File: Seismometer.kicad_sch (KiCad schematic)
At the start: 32 parts

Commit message: Finishing schematic
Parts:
- removed R?: 51, symbol Device:R
- removed R?: R, symbol Device:R
- removed U?: ESP32-WROOM-32, RF_Module:ESP32-WROOM-32, symbol RF_Module:ESP32-WROOM-32
- added C1, C2, C3, C4: 100n, Capacitor_SMD:C_0603_1608Metric_Pad1.08x0.95mm_HandSolder, symbol Device:C
- added R1, R2: 10k, Resistor_SMD:R_0603_1608Metric, symbol Device:R
- added R10, R11, R12, R13, R14, R15, R16, R17, R18, R19, R20, R21, R22, R23, R24, R25, R26, R27, R28, R29, R31, R32, R33, R34, R35, R36, R37, R38, R39, R4, R5, R6, R7, R8, R9: 51, Resistor_SMD:R_0603_1608Metric, symbol Device:R
- added R3, R30: 100k, Resistor_SMD:R_0603_1608Metric, symbol Device:R
- added U1: DLVR-F50D, Package_DIP:DIP-8_W8.89mm_SMDSocket_LongPads, symbol seismometer:DLVR
- C10, C11, C13, C6, C7, C8: renamed from C?; footprint (none) -> Capacitor_SMD:C_0603_1608Metric_Pad1.08x0.95mm_HandSolder
- C12, C14, C15, C5, C9: renamed from C?; footprint (none) -> Capacitor_SMD:C_0805_2012Metric
- FB1, FB2: renamed from FB?; footprint (none) -> Inductor_SMD:L_0805_2012Metric
- R40, R41, R43, R44, R45, R46, R47, R48, R49, R50: renamed from R?; footprint (none) -> Resistor_SMD:R_0603_1608Metric
- R42: renamed from R?; value 51 -> 100k; footprint (none) -> Resistor_SMD:R_0603_1608Metric
- U5: renamed from U?; footprint (none) -> seismometer:Teensy41
- gave numbers to parts that had none: 4
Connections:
- net +3V3: now also C13.1, R49.1, X1.4 (Vdd), C1.1, R1.2, R2.2, R3.2, U1.2 (VSS)
- net GND: now also U3.10 (AIN3P), U3.9 (AIN3N), U5.1 (GND), U5.34 (GND), U5.47 (GND), C1.2, C2.2, C3.2, C4.2, R10.1, R11.1, R12.1, R13.1, R14.1, R15.1, R16.1, R17.1, R18.1, R19.1, R20.1, R21.1, R22.1, R23.2, R24.2, R25.2, R26.2, R27.2, R28.2, R29.2, R30.1, R31.2, R32.2, R33.2, R34.2, R35.2, R36.2, R37.2, R38.2, R7.1, R8.1, R9.1, U1.1 (GND)
- net MISO: now also R45.2, U5.14 (12_MISO_MQSL)
- net MOSI: now also R50.1, U3.16 (DIN)
- net SCK: now also U3.14 (SCLK), R4.2
- net at R47.2: now also U5.20 (28_RX7); no longer U5.18 (26_A12_MOSI1)
- net at U2.11 (~{INT2}): now also R30.2
- net INT_ACCEL: now reaches R43.2
- net INT_ACCEL: now also U5.2 (0_RX1_CRX2_CS1)
- net at U5.10 (8_TX2_IN1): now also R13.2
- net at U5.11 (9_OUT1C): now also R14.2
- net at U5.12 (10_CS_MQSR): now also R15.2
- net 3V3_TEENSY: now reaches U5.15 (3V3)
- net 3V3_TEENSY: now also U5.46 (3V3), C3.1, C4.1
- net at U5.16 (24_A10_TX6_SCL2): now also R46.2
- net at U5.17 (25_A11_RX6_SDA2): now also R16.2
- net at U5.19 (27_A13_SCK1): now also R18.2
- net at U5.21 (29_TX7): now also R19.2
- net at U5.22 (30_CRX3): now also R20.2
- net at U5.23 (31_CTX3): now also R21.2
- net at U5.24 (32_OUT1B): now also R22.2
- net at U5.25 (33_MCLK2): now also R23.1
- net at U5.26 (34_RX8): now also R24.1
- net at U5.27 (35_TX8): now also R25.1
- net at U5.28 (36_CS): now also R6.1
- net at U5.29 (37_CS): now also R5.1
- net INT_DLVR: now reaches U5.3 (1_TX1_CTX2_MISO1)
- net INT_DLVR: now also R3.1, R39.1
- net at U5.30 (38_CS1_IN1): now also R26.1
- net at U5.31 (39_MISO1_OUT1A): now also R27.1
- net at U5.32 (40_A16): now also R28.1
- net at U5.33 (41_A17): now also R29.1
- net at U5.35 (13_SCK_LED): now also R4.1
- net at U5.36 (14_A0_TX3_SPDIF_OUT): now also R31.1
- net at U5.37 (15_A1_RX3_SPDIF_IN): now also R32.1
- net at U5.38 (16_A2_RX4_SCL1): now also R33.1
- net at U5.39 (17_A3_TX4_SDA1): now also R34.1
- net at U5.4 (2_OUT2): now also R7.2
- net SDA: now reaches U5.40 (18_A4_SDA)
- net SDA: now also R2.1, U1.3 (SDA/MISO)
- net SCL: now reaches U5.41 (19_A5_SCL)
- net SCL: now also R1.1, U1.4 (SCL/SCKL)
- net at U5.42 (20_A6_TX5_LRCLK1): now also R35.1
- net at U5.43 (21_A7_RX5_BCLK1): now also R36.1
- net at U5.44 (22_A8_CTX1): now also R37.1
- net at U5.45 (23_A9_CRX1_MCLK1): now also R38.1
- net at U5.48 (VIN): now also C2.1
- net at U5.5 (3_LRCLK2): now also R8.2
- net at U5.6 (4_BCLK2): now also R9.2
- net at U5.7 (5_IN2): now also R10.2
- net at U5.8 (6_OUT1D): now also R11.2
- net at U5.9 (7_RX2_OUT1A): now also R12.2
- net ~{CS_ADC}: now reaches U3.12 (CS)
- net ~{CS_ADC}: now also R6.2
- net ~{CS ACCEL} renamed ~{CS_ACCEL}
- net ~{CS_ACCEL}: now also R5.2
- new net: R17.2, U5.18 (26_A12_MOSI1)
- new net: R39.2, U1.5 (INT/SS)
- now unconnected: U2.10 (NC), U2.5 (NC), U2.8 (NC)
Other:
- moved on the sheet: C11, C12, C13, C14, C15, FB2, R44, R46, R47, R48, R49, R50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

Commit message: Layout
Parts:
- FB1, FB2: value FerriteBead_Small -> MPZ1608S102ATA00; MANUFACTURER (none) -> TDK
- R41: value 4k7 -> 100k
- U2: footprint MC3479:PQFN50P200X200X100-12N -> seismometer:PQFN50P200X200X100-12N
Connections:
- net at C15.1, FB2.1: now also C2.1, U5.48 (VIN); no longer U5.49 (VUSB)
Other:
- moved on the sheet: C7, FB1

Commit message: Initial layout complete
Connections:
- net GND: now also C4.1, R25.1, R6.1; no longer C4.2, R21.1, R25.2
- net INT_ACCEL: now also U5.24 (32_OUT1B); no longer U5.2 (0_RX1_CRX2_CS1)
- net ~{CS_ACCEL}: now also R21.1; no longer R5.2
- net ~{CS_ADC}: now also R5.2; no longer R6.2
- net at U5.20 (28_RX7): now also R6.2; no longer R47.2
- net ADC_SYNC/RESET: now reaches U5.28 (36_CS)
- net ADC_SYNC/RESET: now also R47.2; no longer R6.1
- net at U5.16 (24_A10_TX6_SCL2): now also R25.2; no longer R46.2
- net at R22.2: now also U5.2 (0_RX1_CRX2_CS1); no longer U5.24 (32_OUT1B)
- net ADC_DRDY: now reaches U5.27 (35_TX8)
- net ADC_DRDY: now also R46.2; no longer R25.1
- net 3V3_TEENSY: no longer names the net of C3.1, U5.46 (3V3)
- net 3V3_TEENSY: no longer C4.1, U5.15 (3V3)
- new net: C4.2, U5.15 (3V3)
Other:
- moved on the sheet: C3, C4, R5, R50, R6

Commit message: Ready
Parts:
- C1, C10, C13, C2, C3, C4, C6, C7: MANUFACTURER (none) -> KEMET; MP (none) -> CGA3E3X7R1H224K080AB
- C11: value 10p -> 12p; MANUFACTURER (none) -> KEMET; MP (none) -> C0603C120J5GACTU
- C12, C14, C15, C5, C9: MANUFACTURER (none) -> YAEGO; MP (none) -> CC0402KRX5R6BB105
- C8: MANUFACTURER (none) -> TDK; MP (none) -> CGA3E3X7R1H224K080AB
- FB1, FB2: MP (none) -> MPZ1608S102ATA00
- R1, R2: MANUFACTURER (none) -> PANASONIC; MP (none) -> ERJ3EKF1002V
- R10, R11, R12, R13, R14, R15, R16, R17, R18, R19, R20, R21, R22, R23, R24, R25, R26, R27, R28, R29, R31, R32, R33, R34, R35, R36, R37, R38, R39, R4, R40, R43, R45, R46, R47, R5, R50, R6, R7, R8, R9: MANUFACTURER (none) -> YAGEO; MP (none) -> RC0603FR-0751RL
- R3, R30, R41, R42, R48, R49: MANUFACTURER (none) -> VISHAY; MP (none) -> CRCW0603100KFKEA
- R44: MANUFACTURER (none) -> VISHAY; MP (none) -> CRCW060310R0FKEA
- U1: MANUFACTURER (none) -> AllSensors; MP (none) -> DLVR-F50D; now not fitted; now left out of the parts list
- U2: Purchase-URL https://www.snapeda.com/api/url_track_click_mouser/?unipart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 -> (none); SnapEDA_Link https://www.snapeda.com/parts/MC3479/Memsic/view-part/?ref=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 -> (none)
- U3: MANUFACTURER (none) -> Texas Instruments; MP (none) -> ADS131M04-Q1
- U4: MANUFACTURER (none) -> Texas Instruments; MP (none) -> LP5907MFX-3.3
- U5: MANUFACTURER (none) -> PRJC; now not fitted; now left out of the parts list
- X1: value ASE-xxxMHz -> SIT8924BA-22-33E-8.192000G; MANUFACTURER (none) -> SiTime; MP (none) -> SIT8924BA-22-33E-8.192000G

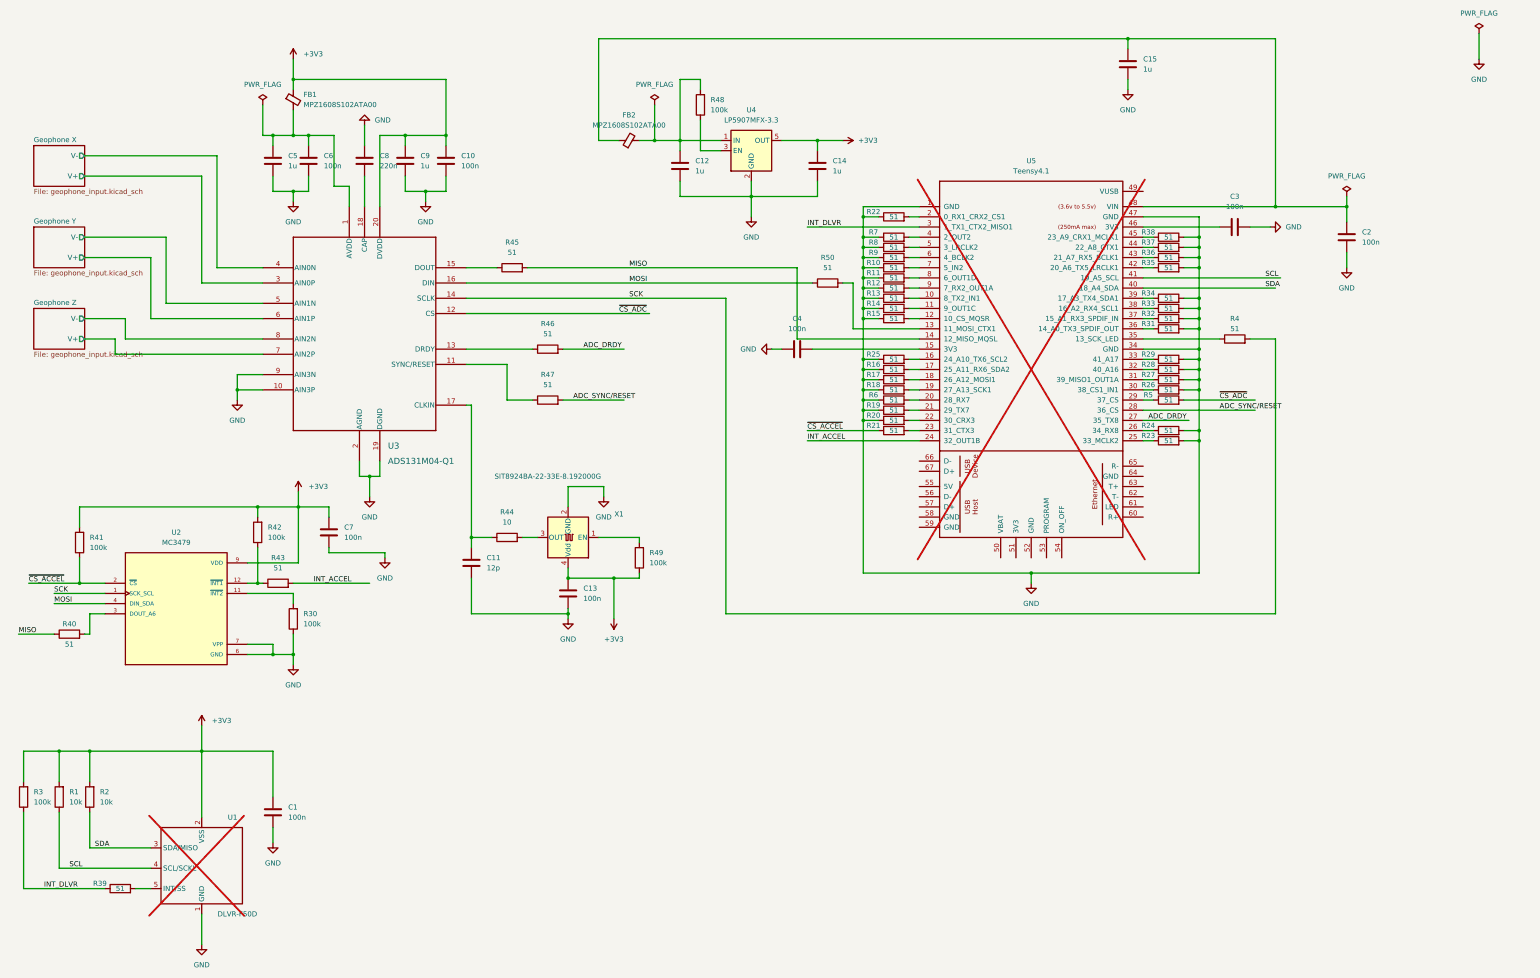
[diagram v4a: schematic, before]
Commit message: Active input filter
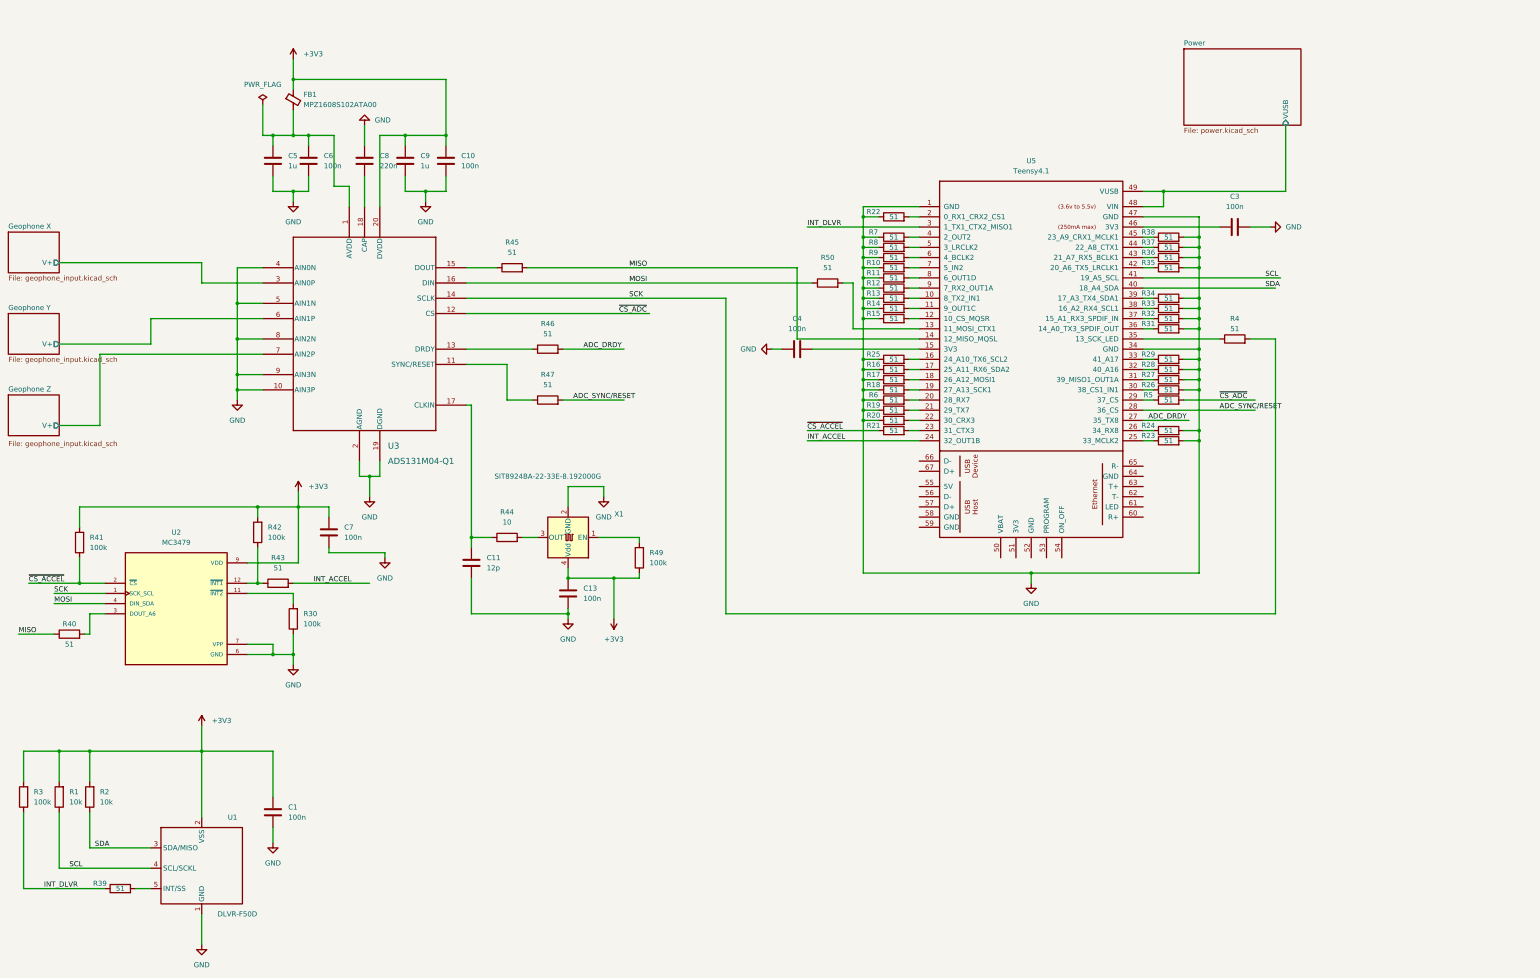
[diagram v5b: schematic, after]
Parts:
- removed C12, C14, C15: 1u, Capacitor_SMD:C_0805_2012Metric, symbol Device:C
- removed C2: 100n, Capacitor_SMD:C_0603_1608Metric_Pad1.08x0.95mm_HandSolder, symbol Device:C
- removed FB2: MPZ1608S102ATA00, Inductor_SMD:L_0805_2012Metric, symbol Device:FerriteBead_Small
- removed R48: 100k, Resistor_SMD:R_0603_1608Metric, symbol Device:R
- removed U4: LP5907MFX-3.3, Package_TO_SOT_SMD:SOT-23-5, symbol Regulator_Linear:LP5907MFX-3.3
- U1, U5: now fitted
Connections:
- net Geophone X/V- is gone; now on net GND: U3.4 (AIN0N)
- net Geophone Y/V- is gone; now on net GND: U3.5 (AIN1N)
- net Geophone Z/V- is gone; now on net GND: U3.8 (AIN2N)
- net Power/VUSB: now reaches U5.48 (VIN)
- net Power/VUSB: now also U5.49 (VUSB)
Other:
- added sheet Power (power.kicad_sch)
- sheet Geophone X ports: added none; removed V-
- sheet Geophone Y ports: added none; removed V-
- sheet Geophone Z ports: added none; removed V-

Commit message: wip Layout
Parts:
- removed R10, R11, R12, R13, R14, R15, R16, R17, R18, R19, R20, R22, R23, R24, R25, R26, R27, R28, R29, R31, R32, R33, R34, R35, R36, R37, R38, R47, R7, R8, R9: 51, Resistor_SMD:R_0603_1608Metric, symbol Device:R
- C5, C9: footprint Capacitor_SMD:C_0805_2012Metric -> Capacitor_SMD:C_1206_3216Metric
- U2: Purchase-URL (none) -> https://www.snapeda.com/api/url_track_click_mouser/?unipart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; SnapEDA_Link (none) -> https://www.snapeda.com/parts/MC3479/Memsic/view-part/?ref=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
- U5: symbol seismometer:Teensy4.1 -> seismometer:Teensy4.1_minimal; now in the parts list
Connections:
- net ADC_SYNC/RESET: now also R6.2, U3.11 (SYNC/RESET); no longer U5.28 (36_CS)
- net GND: now also U5.52 (GND); no longer R6.1
- net at U5.20 (28_RX7): no longer R6.2
- new net: R6.1, U5.28 (36_CS)
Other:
- note added: "Unconnected IO pins tied low in SW"

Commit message: Layout done. Tweaking...
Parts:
- removed R21: 51, Resistor_SMD:R_0603_1608Metric, symbol Device:R
- added C62: 1u, Capacitor_SMD:C_1206_3216Metric, symbol Device:C
- added R7: 51, Resistor_SMD:R_0603_1608Metric, symbol Device:R
- U5: footprint seismometer:Teensy41 -> seismometer:Teensy41_minimal
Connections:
- net +3V3: now also C62.1
- net ADC_DRDY: now also U5.36 (14_A0_TX3_SPDIF_OUT); no longer U5.27 (35_TX8)
- net GND: now also C62.2; no longer U5.52 (GND)
- net INT_ACCEL: now also U5.43 (21_A7_RX5_BCLK1); no longer U5.24 (32_OUT1B)
- net INT_DLVR: now also U5.39 (17_A3_TX4_SDA1); no longer U5.3 (1_TX1_CTX2_MISO1)
- net Power/VUSB: no longer U5.49 (VUSB)
- net ~{CS_ACCEL}: now also R7.1
- net at U5.29 (37_CS): no longer R5.1
- net at R6.1: now also U5.37 (15_A1_RX3_SPDIF_IN); no longer U5.28 (36_CS)
- net at U5.38 (16_A2_RX4_SCL1): now also R5.1
- net at U5.42 (20_A6_TX5_LRCLK1): now also R7.2
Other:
- moved on the sheet: R4, R6
